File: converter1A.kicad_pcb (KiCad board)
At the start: 2 copper layers, 30 parts, among them IC1 LMR50410YQDBVRQ1, IC3 LMR50410YQDBVRQ1, IC4 LM2678S-12_NOPB, J1 Pin entree 15V, J13 Pin entree 15V, J2 Pin entrée 15V, J3 Pin sortie 3.3V, J4 pin sortie 5V, J5 Conn_01x16_Pin

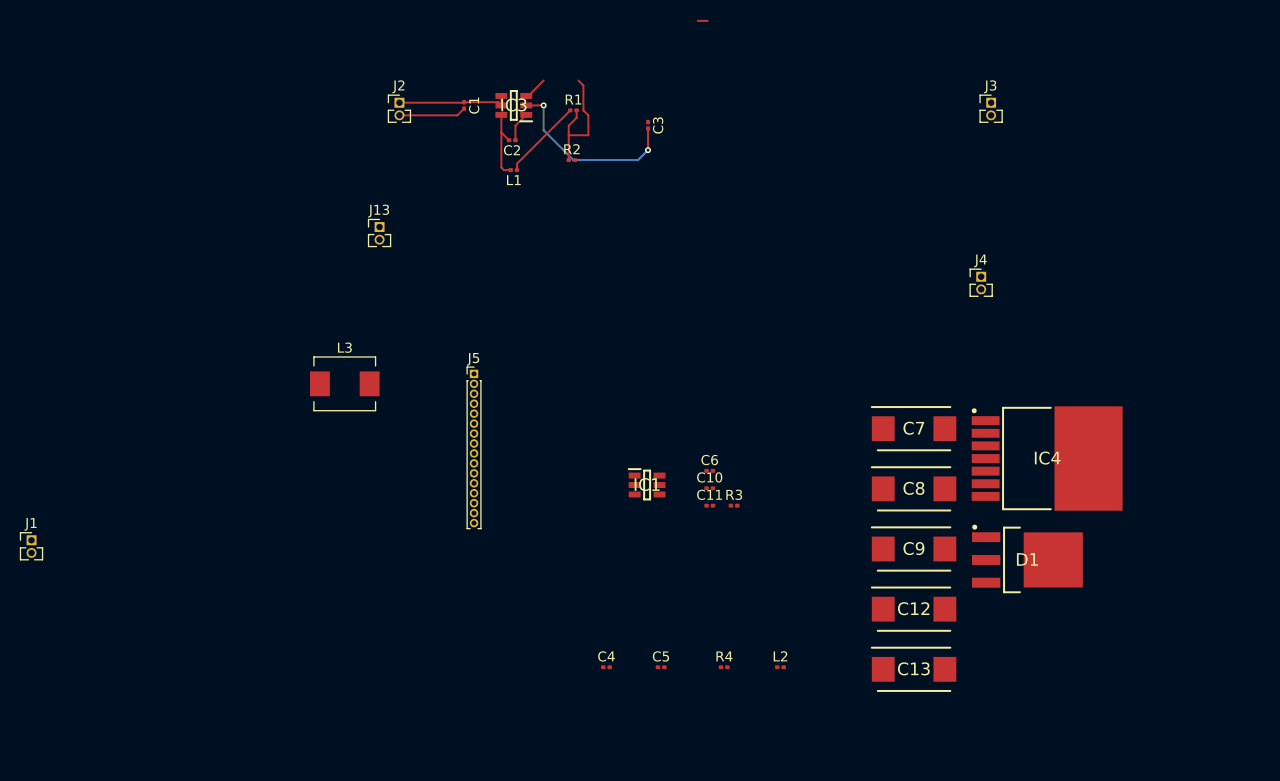
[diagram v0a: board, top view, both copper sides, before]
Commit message: the power board
maybe the component will not be right
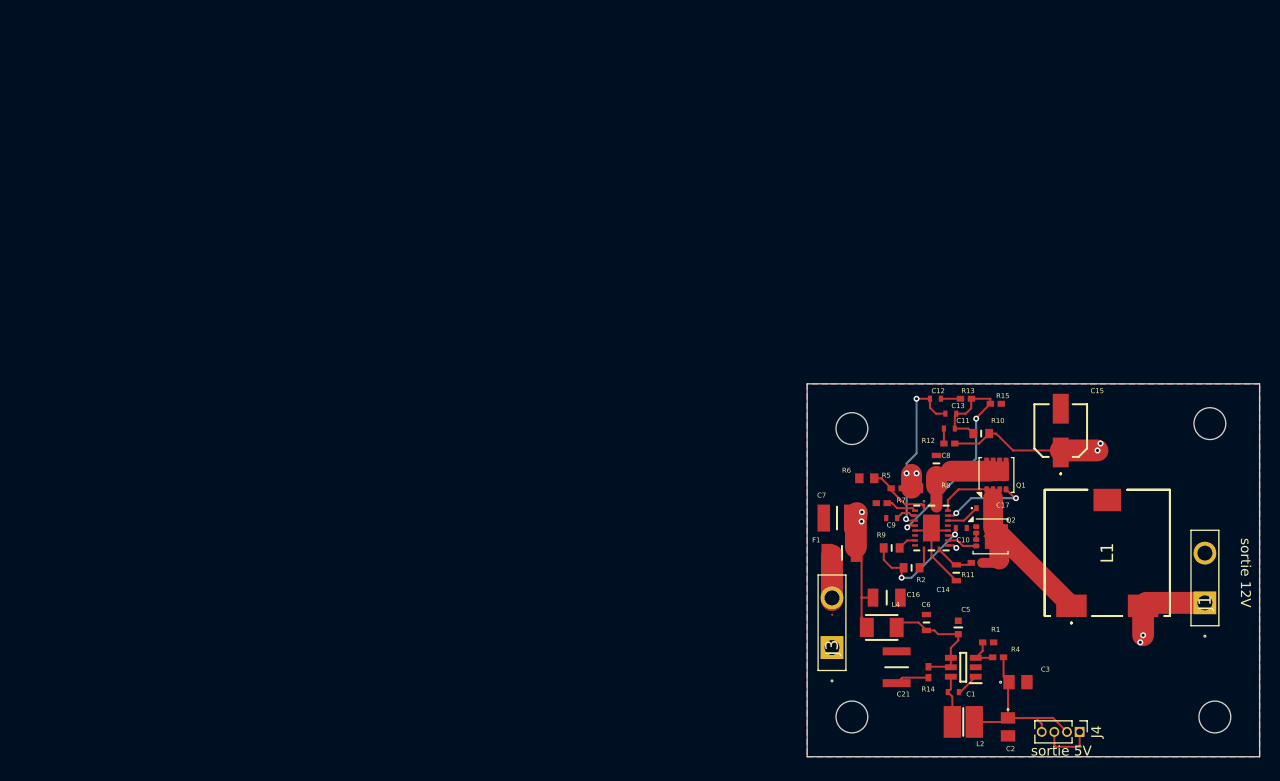
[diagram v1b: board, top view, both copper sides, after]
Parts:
- removed C4: 10uF, Capacitor_SMD:C_0201_0603Metric
- removed D1: MBRD835LT4G, diode:TO229P990X238-4N
- removed IC1: LMR50410YQDBVRQ1, converter:SOT95P280X145-6N
- removed IC4: LM2678S-12_NOPB, converter:TO127P1435X464-8N
- removed J13: Pin entree 15V, Connector_PinHeader_1.27mm:PinHeader_1x02_P1.27mm_Vertical
- removed J2: Pin entrée 15V, Connector_PinHeader_1.27mm:PinHeader_1x02_P1.27mm_Vertical
- removed J5: Conn_01x16_Pin, Connector_PinHeader_1.00mm:PinHeader_1x16_P1.00mm_Vertical
- removed L3: 15uH, Inductor_SMD:L_Neosid_SM-PIC0512H
- removed R3: 87.7k, Resistor_SMD:R_0201_0603Metric
- added C14: GRM1885C2A100JA01D, 12V Power Board composants:CAPC1608X90N, F.Cu at (179.0, 93.0)
- added C15: 20SVPF56MX, 12V Power Board composants:16SVF82M, F.Cu at (189.5, 78.7)
- added C16: GRM31CR71H475KA12L, 12V Power Board composants:CAPC3216X180N, F.Cu at (172.0, 95.5)
- added C17: GCM1555C1H100FA16D, 12V Power Board composants:GCM155, F.Cu at (181.5, 86.5)
- added C21: C3225X7S2A475M200AB, 12V Power Board composants:CAPC3225X200N, F.Cu at (173.0, 102.5)
- added F1: SF-1206HH12M-2, 12V Power Board composants:FUSC3216X117N, F.Cu at (167.5, 91.0)
- added H1: MountingHole, MountingHole:MountingHole_3.2mm_M3, F.Cu at (168.5, 78.5)
- added H2: MountingHole, MountingHole:MountingHole_3.2mm_M3, F.Cu at (204.5, 78.0)
- added H3: MountingHole, MountingHole:MountingHole_3.2mm_M3, F.Cu at (168.5, 107.5)
- added H4: MountingHole, MountingHole:MountingHole_3.2mm_M3, F.Cu at (205.0, 107.5)
- added IC2: LM25145RGYR, 12V Power Board composants:RGY0020B, F.Cu at (176.5, 88.5)
- added L4: NLCV32T-R33M-EFRD, 12V Power Board composants:INDPM3225X240N, F.Cu at (171.5, 98.5)
- added Q1: CSD17577Q3A, Package_SON:VSON-8_3.3x3.3mm_P0.65mm_NexFET, F.Cu at (183.0, 83.2)
- added Q2: CSD17577Q3A, Package_SON:VSON-8_3.3x3.3mm_P0.65mm_NexFET, F.Cu at (182.4, 89.3)
- added R10: RC0603FR-0718KL, 12V Power Board composants:RESC1608X55N, F.Cu at (181.5, 79.0)
- added R11: CRCW04021K24FKED, 12V Power Board composants:RESC1005X40N, F.Cu at (181.1, 92.0)
- added R12: CRCW04022K49FKED, 12V Power Board composants:RESC1005X40N, F.Cu at (178.3, 80.0)
- added R13: CRCW04022K37FKED, 12V Power Board composants:RESC1005X40N, F.Cu at (180.0, 75.5)
- added R14: CRCW04021R00FKED, 12V Power Board composants:RESC1005X40N, F.Cu at (176.2, 103.0)
- added R15: CRCW04021K27FKED, 12V Power Board composants:RESC1005X40N, F.Cu at (183.0, 76.0)
- added R5: CRCW040269K8FKED, 12V Power Board composants:RESC1005X40N, F.Cu at (173.0, 84.5)
- added R6: CRCW06038K25FKEA, 12V Power Board composants:RESC1608X50N, F.Cu at (170.0, 83.5)
- added R7: CRCW040239K2FKED, 12V Power Board composants:RESC1005X40N, F.Cu at (171.5, 86.0)
- added R8: CRCW06032R10FKEA, 12V Power Board composants:RESC1608X50N, F.Cu at (176.0, 84.5)
- added R9: RC0603FR-0720KL, 12V Power Board composants:RESC1608X55N, F.Cu at (172.5, 90.5)
- C1: value 2.2uF -> GRM155R71C104KA88D; footprint Capacitor_SMD:C_0201_0603Metric -> 12V Power Board composants:CAPC1005X55N
- C10: value 0.47uF -> C1005X5R1V225K050BC; footprint Capacitor_SMD:C_0201_0603Metric -> 12V Power Board composants:CAPC1005X55N
- C11: value 0.01uF -> CGA2B2X7R1H681K050BA; footprint Capacitor_SMD:C_0201_0603Metric -> 12V Power Board composants:CAPC1005X55N
- C12: value TAJE686M020RNJ -> GRM155R71C822KA01D; footprint capa:capa 68uF AVX -> 12V Power Board composants:CAPC1005X55N
- C13: value TAJE686M020RNJ -> CGA2B2X7R1H681K050BA; footprint capa:capa 68uF AVX -> 12V Power Board composants:CAPC1005X55N
- C2: value 0.1uF -> C0805C106K8PACTU; footprint Capacitor_SMD:C_0201_0603Metric -> 12V Power Board composants:C0805
- C3: value 10uF -> C0805C106K8PACTU; footprint Capacitor_SMD:C_0201_0603Metric -> 12V Power Board composants:C0805
- C5: value 0.1uF -> GRM188R72A104KA35J; footprint Capacitor_SMD:C_0201_0603Metric -> 12V Power Board composants:GRM18x
- C6: value 2.2uF -> C1608X5R1E106M080AC; footprint Capacitor_SMD:C_0201_0603Metric -> 12V Power Board composants:CAPC1608X80N
- C7: value TPSD336M020R0200 -> GRM32ER71H475KA88L; footprint capa:CAPPM7344X310N -> 12V Power Board composants:CAPC3225X270N
- C8: value TPSD336M020R0200 -> CGA3E2X7R1H104K080AA; footprint capa:CAPPM7344X310N -> 12V Power Board composants:CAPC1608X90N
- C9: value TPSD336M020R0200 -> GRM155R71C563KA88D; footprint capa:CAPPM7344X310N -> 12V Power Board composants:CAPC1005X55N
- J1: value Pin entree 15V -> 1933189; footprint Connector_PinHeader_1.27mm:PinHeader_1x02_P1.27mm_Vertical -> 12V Power Board composants:1933189
- J3: value Pin sortie 3.3V -> 1933189; footprint Connector_PinHeader_1.27mm:PinHeader_1x02_P1.27mm_Vertical -> 12V Power Board composants:1933189
- J4: value pin sortie 5V -> Conn_01x04_Pin; footprint Connector_PinHeader_1.27mm:PinHeader_1x02_P1.27mm_Vertical -> Connector_PinHeader_1.27mm:PinHeader_1x04_P1.27mm_Vertical
- L1: value 3.3uH -> SER1360-272KLD; footprint Inductor_SMD:L_0201_0603Metric -> 12V Power Board composants:SER1360272KLD
- L2: value 4.7uH -> 74438336047; footprint Inductor_SMD:L_0201_0603Metric -> 12V Power Board composants:INDC3030X200N
- R1: value 51k -> CRCW040222K1FKED; footprint Resistor_SMD:R_0201_0603Metric -> 12V Power Board composants:RESC1005X40N
- R2: value 22.1k -> RC0603FR-0720KL; footprint Resistor_SMD:R_0201_0603Metric -> 12V Power Board composants:RESC1608X55N
- R4: value 22.1k -> CRCW040288K7FKED; footprint Resistor_SMD:R_0201_0603Metric -> 12V Power Board composants:RESC1005X40N
- moved J1 118.2 mm to (204.0, 96.0), turned to 90 degrees
- moved C2 77.2 mm to (184.2, 108.5), turned to -90 degrees
- moved C1 76.8 mm to (178.7, 105.0), turned to 0 degrees
- moved IC3 72.4 mm to (179.7, 102.5)
- moved L1 71.0 mm to (194.2, 91.0), turned to 90 degrees
- moved R1 67.8 mm to (182.2, 100.0)
- moved C3 67.2 mm to (185.2, 104.0), turned to 0 degrees
- moved J3 57.1 mm to (166.5, 100.5), turned to 90 degrees
- moved R2 53.4 mm to (174.5, 92.5)
- moved J4 46.8 mm to (191.4, 109.0), turned to -90 degrees
- moved C5 30.1 mm to (179.2, 98.5), turned to 90 degrees
- moved R4 27.6 mm to (183.2, 101.5), turned to 180 degrees
- moved C6 26.6 mm to (176.0, 98.0), turned to 90 degrees
- moved C13 26.0 mm to (178.4, 77.0)
- moved C10 25.6 mm to (179.5, 88.5)
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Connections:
- C1 pad 1: Net-(IC3-EN) -> Net-(IC3-SW)
- C1 pad 2: GND -> Net-(IC3-CB)
- C10 pad 1: Net-(C7-+) -> Net-(IC2-VCC)
- C11 pad 2: Net-(D1-A_2) -> Net-(IC2-FB)
- C12 pad 2: GND -> Net-(C12-Pad2)
- C13 pad 2: GND -> Net-(IC2-FB)
- C2 pad 1: Net-(IC3-CB) -> Net-(J4-Pin_2)
- C2 pad 2: Net-(IC3-SW) -> GND
- C3 pad 1: Net-(J3-Pin_1) -> Net-(J4-Pin_2)
- C5 pad 1: Net-(IC1-CB) -> Net-(IC3-EN)
- C5 pad 2: Net-(IC1-SW) -> GND
- C6 pad 1: Net-(IC1-EN) -> Net-(IC3-EN)
- C7 pad 1: Net-(C7-+) -> Net-(C16-Pad1)
- C8 pad 1: Net-(C7-+) -> Net-(IC2-VIN)
- C9 pad 1: Net-(C7-+) -> Net-(IC2-SS/TRK)
- J1 pad 1: GND -> Net-(C15-+)
- J1 pad 2: Net-(IC1-EN) -> GND
- J3 pad 1: Net-(J3-Pin_1) -> GND
- J3 pad 2: GND -> Net-(F1-Pad1)
- J4 pad 1: Net-(J4-Pin_1) -> GND
- J4 pad 2: GND -> Net-(J4-Pin_2)
- L1 pad 1: Net-(J3-Pin_1) -> Net-(IC2-SW)
- L1 pad 2: Net-(IC3-SW) -> Net-(C15-+)
- L2 pad 1: Net-(J4-Pin_1) -> Net-(IC3-SW)
- L2 pad 2: Net-(IC1-SW) -> Net-(J4-Pin_2)
- R1 pad 1: Net-(J3-Pin_1) -> Net-(IC3-FB)
- R1 pad 2: Net-(IC3-FB) -> GND
- R2 pad 1: Net-(IC3-FB) -> Net-(IC2-VCC)
- R2 pad 2: GND -> Net-(IC2-PGOOD)
- R4 pad 1: Net-(IC1-FB) -> Net-(J4-Pin_2)
- R4 pad 2: GND -> Net-(IC3-FB)
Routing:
- net Net-(C15-+): track 0.00 -> 49.2 mm, vias 0 -> 4
- net Net-(IC2-SW): track 0.00 -> 25.3 mm
- net Net-(IC2-FB): track 0.00 -> 25.1 mm, vias 0 -> 2
- net Net-(C16-Pad1): track 0.00 -> 22.5 mm, vias 0 -> 4
- net Net-(J4-Pin_2): track 0.00 -> 18.1 mm
- net Net-(IC2-COMP): track 0.00 -> 17.6 mm, vias 0 -> 2
- net Net-(IC2-VCC): track 0.00 -> 13.4 mm, vias 0 -> 2
- net Net-(IC3-FB): track 15.6 -> 3.56 mm
- net Net-(IC2-VIN): track 0.00 -> 9.66 mm
- net Net-(J3-Pin_1): track 9.22 -> 0.00 mm
- net Net-(IC2-HO): track 0.00 -> 8.95 mm, vias 0 -> 2
- net GND: track 25.4 -> 17.1 mm, vias 2 -> 1
- net Net-(IC2-EN/UVLO): track 0.00 -> 6.31 mm
- net Net-(IC2-ILIM): track 0.00 -> 3.97 mm
- net Net-(C21-Pad1): track 0.00 -> 3.48 mm
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- added copper zone on B.Cu, net GND
- added copper zone on F.Cu, net GND
- added copper zone on In1.Cu, net GND
- added copper zone on In2.Cu, net GND
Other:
- board outline added: 45.5 x 37.5 mm
- copper layers 2 -> 4
- board text added: "C1"
- board text added: "C10"
- board text added: "C11"
- board text added: "C12"
- board text added: "C13"
- board text added: "C14"
- board text added: "C15"
- board text added: "C16"
- board text added: "C17"
- board text added: "C2"
- board text added: "C21"
- board text added: "C3"
- board text added: "C5"
- board text added: "C6"
- board text added: "C7"
- board text added: "C8"
- board text added: "C9"
- board text added: "F1"
- board text added: "L2"
- board text added: "L4"
- board text added: "Q1"
- board text added: "Q2"
- board text added: "R1"
- board text added: "R10"
- board text added: "R11"
- board text added: "R12"
- board text added: "R13"
- board text added: "R14"
- board text added: "R15"
- board text added: "R2"
- board text added: "R4"
- board text added: "R5"
- board text added: "R6"
- board text added: "R7"
- board text added: "R8"
- board text added: "R9"
- board text added: "sortie 12V"
- board text added: "sortie 5V"

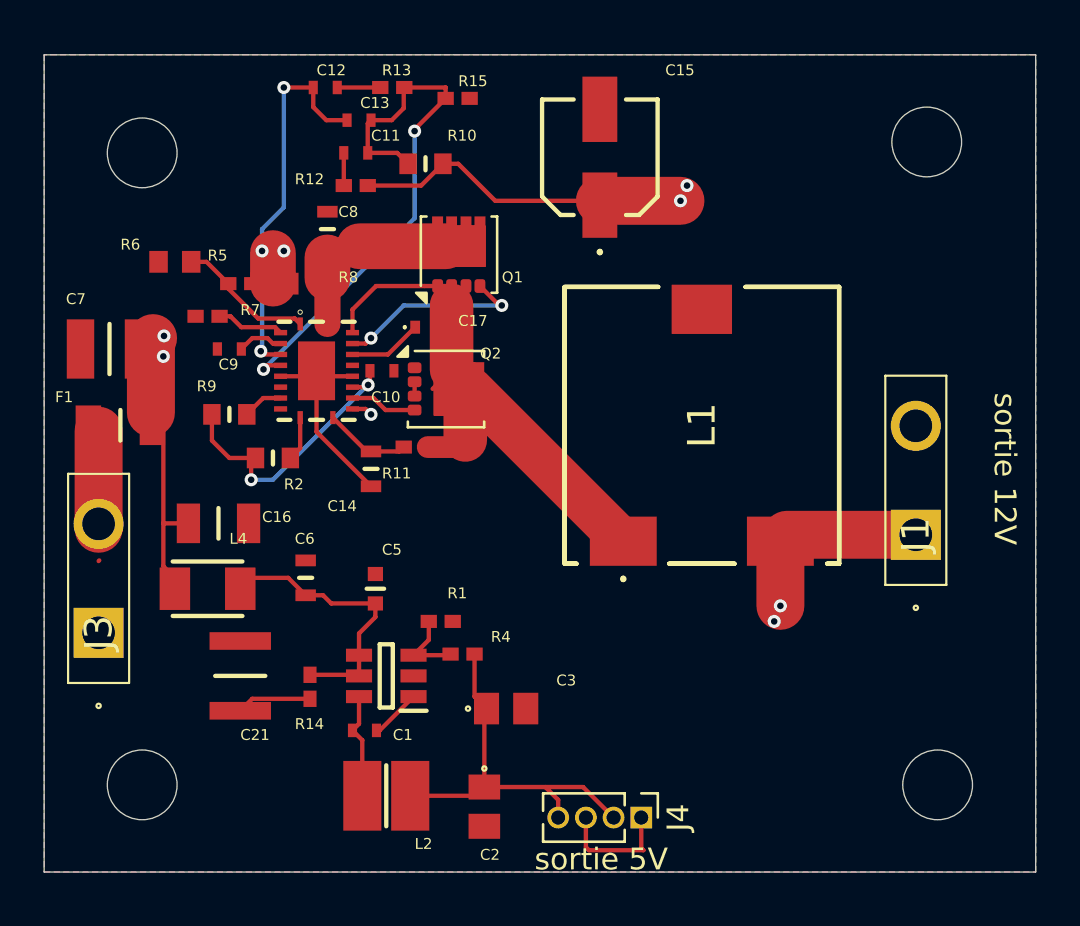
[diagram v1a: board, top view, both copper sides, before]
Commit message: version smaller of the PCB
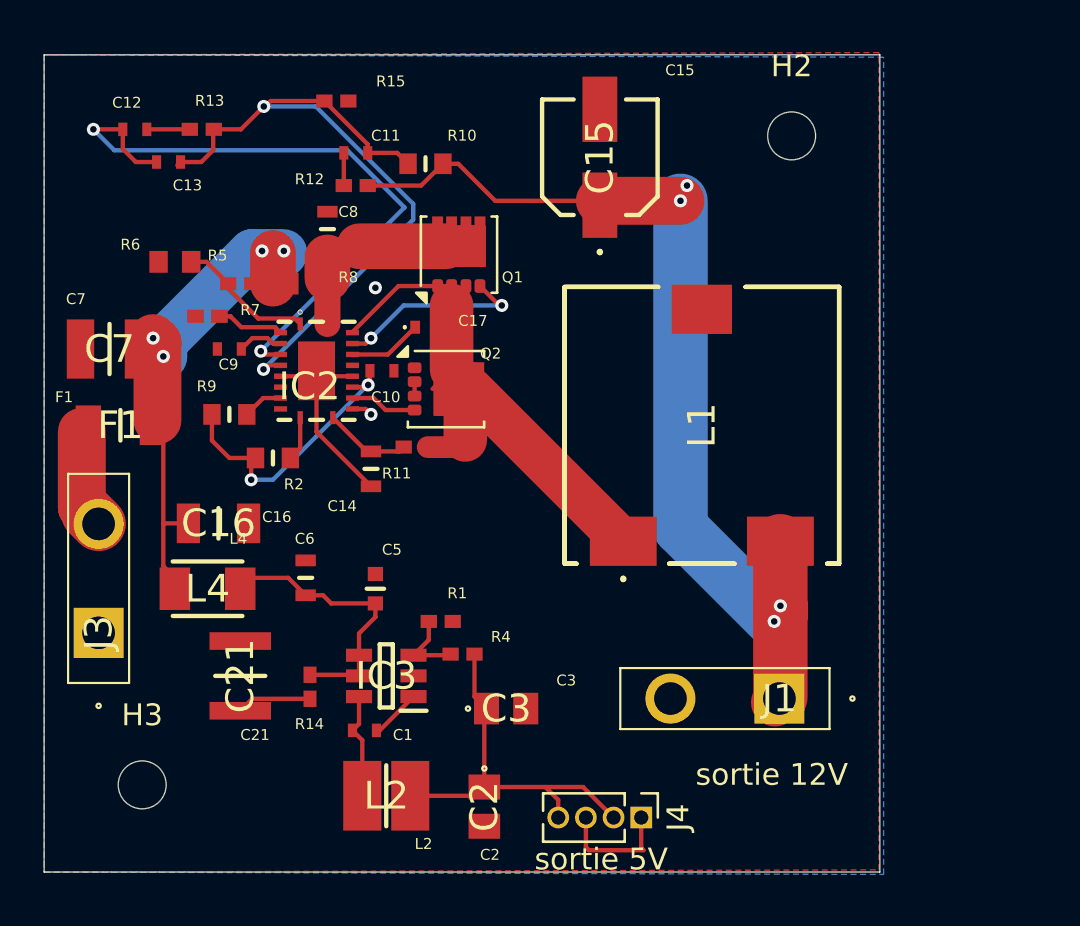
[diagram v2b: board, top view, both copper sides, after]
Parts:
- removed H1, H4: MountingHole, MountingHole:MountingHole_3.2mm_M3
- C3: value C0805C106K8PACTU -> C0805C106K8PACTU (2X)
- H2, H3: footprint MountingHole:MountingHole_3.2mm_M3 -> MountingHole:MountingHole_2.2mm_M2
- moved J1 9.78 mm to (197.7, 103.5), turned to 180 degrees
- moved C12 8.95 mm to (168.2, 77.4)
- moved C13 8.95 mm to (169.7, 78.9)
- moved R13 8.95 mm to (171.2, 77.4)
- moved H2 6.21 mm to (198.3, 77.7)
- moved R15 5.57 mm to (177.4, 76.1)
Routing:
- net Net-(IC2-COMP): track 17.6 -> 30.1 mm
- net Net-(IC2-FB): track 25.1 -> 33.4 mm
- net Net-(F1-Pad1): track 0.08 -> 4.59 mm
- net Net-(C15-+): track 49.2 -> 44.9 mm
- net Net-(C16-Pad1): track 22.5 -> 23.3 mm
- net Net-(IC2-SW): track 25.3 -> 24.7 mm
- net GND: vias 1 -> 2
- removed copper zone on In1.Cu, net GND
- removed copper zone on In2.Cu, net GND
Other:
- board size 45.5 x 37.5 mm -> 38.3 x 37.5 mm
- copper layers 4 -> 2
